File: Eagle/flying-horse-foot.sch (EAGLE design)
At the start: 20 parts, among them U1 8U2-AU, Y1 16MHz

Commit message: rel 1
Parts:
- added S1: MK6-5-B, switch-reed:REED-SWITCH-MK6-5-B
- C4, C6: value 0.1uF -> 1.0uF; device SparkFun-Capacitors:0.1UF-0603-25V-5% -> SparkFun-Capacitors:1.0UF-0603-16V-10%
- C7, C8: value 1.0uF -> 0.1uF; device SparkFun-Capacitors:1.0UF-0603-16V-10% -> SparkFun-Capacitors:0.1UF-0603-25V-5%
- U$1, U$2: value 74HC42 -> 74HC42D16; device aaa2:74HC42 -> aaa2:74HC42D16
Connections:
- removed net N$9: RESET.2, U1.RESET/PC1
- new net RESET: RESET.2, S1.1, U1.RESET/PC1
- net COL-3: no longer U$4.P$13
- net COL-5: now also U$4.P$13
- net GND: now also C5.1, C8.2, S1.2; no longer C5.2, C8.1
- net N$3: now also C2.1; no longer C3.1
- net N$4: now also C3.1; no longer C2.1
- net N$6: now also C4.1; no longer C7.1
- net VCC: now also C5.2, C7.1, C8.1; no longer C4.1, C5.1, C8.2
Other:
- moved on the sheet: C2, C3, C4, C5, C6, C7, C8, R4, R5, RESET

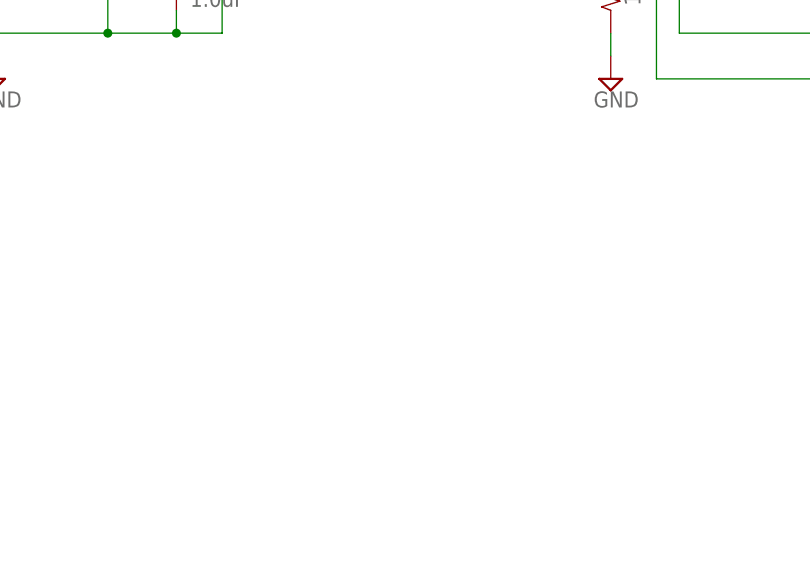
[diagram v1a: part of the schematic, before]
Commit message: made top plane vcc, instead of gnd
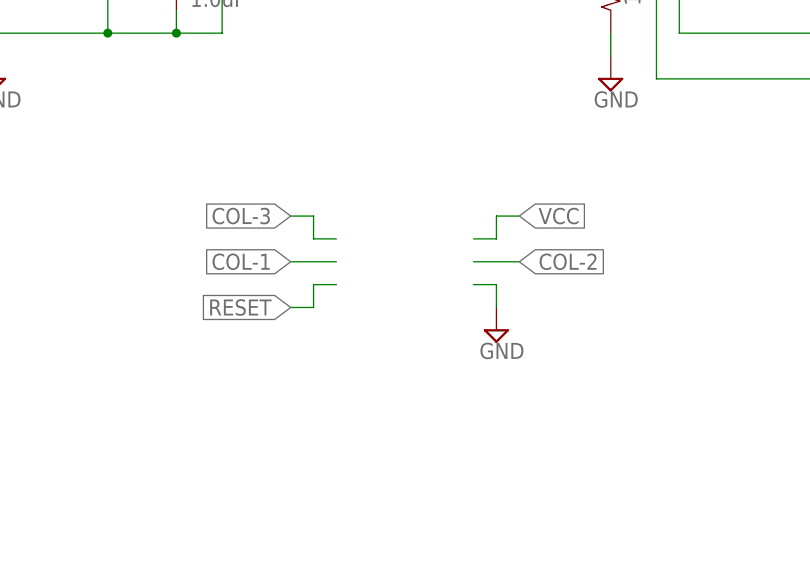
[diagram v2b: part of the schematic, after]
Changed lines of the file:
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@@
 <part name="SUPPLY6" library="supply2" library_urn="urn:adsk.eagle:library:372" deviceset="GND" device=""/>
 <part name="S1" library="switch-reed" library_urn="urn:adsk.eagle:library:379" deviceset="REED-SWITCH-" device="MK6-5-B" package3d_urn="urn:adsk.eagle:package:27524/1" value="MK6-5-B"/>
+<part name="SUPPLY7" library="supply2" library_urn="urn:adsk.eagle:library:372" deviceset="GND" device=""/>
 </parts>
 <sheets>
@@
 <attribute name="NAME" x="160.02" y="167.64" size="1.778" layer="95" rot="R270"/>
 <attribute name="VALUE" x="157.48" y="167.64" size="1.778" layer="96" rot="R270"/>
+</instance>
+<instance part="SUPPLY7" gate="GND" x="208.28" y="43.18" smashed="yes">
+<attribute name="VALUE" x="206.375" y="40.005" size="1.778" layer="96"/>
 </instance>
 </instances>
@@
 <junction x="152.4" y="154.94"/>
 </segment>
+<segment>
+<wire x1="205.74" y1="48.26" x2="208.28" y2="48.26" width="0.1524" layer="91"/>
+<pinref part="SUPPLY7" gate="GND" pin="GND"/>
+<wire x1="208.28" y1="48.26" x2="208.28" y2="45.72" width="0.1524" layer="91"/>
+</segment>
 </net>
 <net name="ROW-B" class="0">
@@
 <pinref part="U$4" gate="G$1" pin="P$5"/>
 </segment>
+<segment>
+<wire x1="205.74" y1="50.8" x2="210.82" y2="50.8" width="0.1524" layer="91"/>
+<label x="210.82" y="50.8" size="1.778" layer="95" xref="yes"/>
+</segment>
 </net>
 <net name="COL-0" class="0">
@@
 <pinref part="U$4" gate="G$1" pin="P$8"/>
 </segment>
+<segment>
+<wire x1="190.5" y1="53.34" x2="187.96" y2="53.34" width="0.1524" layer="91"/>
+<wire x1="187.96" y1="53.34" x2="187.96" y2="55.88" width="0.1524" layer="91"/>
+<wire x1="187.96" y1="55.88" x2="185.42" y2="55.88" width="0.1524" layer="91"/>
+<label x="185.42" y="55.88" size="1.778" layer="95" rot="R180" xref="yes"/>
+</segment>
 </net>
 <net name="COL-1" class="0">
@@
 <label x="45.72" y="78.74" size="1.778" layer="95" xref="yes"/>
 <pinref part="U$4" gate="G$1" pin="P$3"/>
+</segment>
+<segment>
+<wire x1="190.5" y1="50.8" x2="185.42" y2="50.8" width="0.1524" layer="91"/>
+<label x="185.42" y="50.8" size="1.778" layer="95" rot="R180" xref="yes"/>
 </segment>
 </net>
@@
 <junction x="78.74" y="60.96"/>
 </segment>
+<segment>
+<wire x1="205.74" y1="53.34" x2="208.28" y2="53.34" width="0.1524" layer="91"/>
+<wire x1="208.28" y1="53.34" x2="208.28" y2="55.88" width="0.1524" layer="91"/>
+<wire x1="208.28" y1="55.88" x2="210.82" y2="55.88" width="0.1524" layer="91"/>
+<label x="210.82" y="55.88" size="1.778" layer="95" xref="yes"/>
+</segment>
 </net>
 <net name="N$1" class="0">
@@
 <label x="177.8" y="165.1" size="1.778" layer="95" xref="yes"/>
 </segment>
-</net>
+<segment>
+<wire x1="190.5" y1="48.26" x2="187.96" y2="48.26" width="0.1524" layer="91"/>
+<wire x1="187.96" y1="48.26" x2="187.96" y2="45.72" width="0.1524" layer="91"/>
+<wire x1="187.96" y1="45.72" x2="185.42" y2="45.72" width="0.1524" layer="91"/>
+<label x="185.42" y="45.72" size="1.778" layer="95" rot="R180" xref="yes"/>
+</segment>
+</net>

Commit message: prep for board manufacturing
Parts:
- removed Y1: 16MHz, SparkFun-Clocks:CRYSTAL-16MHZSMD-2X1.6
- added Y2: 16MHz, SparkFun-Clocks:CRYSTAL-16MHZSMD-5X3.2
- C1: device SparkFun-Capacitors:10UF-POLAR-EIA3216-16V-10%(TANT) -> aaa2:EEE-1CA100SR-EIA3528-20V-10%(TANT)
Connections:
- net N$3: now also Y2.2; no longer Y1.2
- net N$4: now also Y2.1; no longer Y1.1

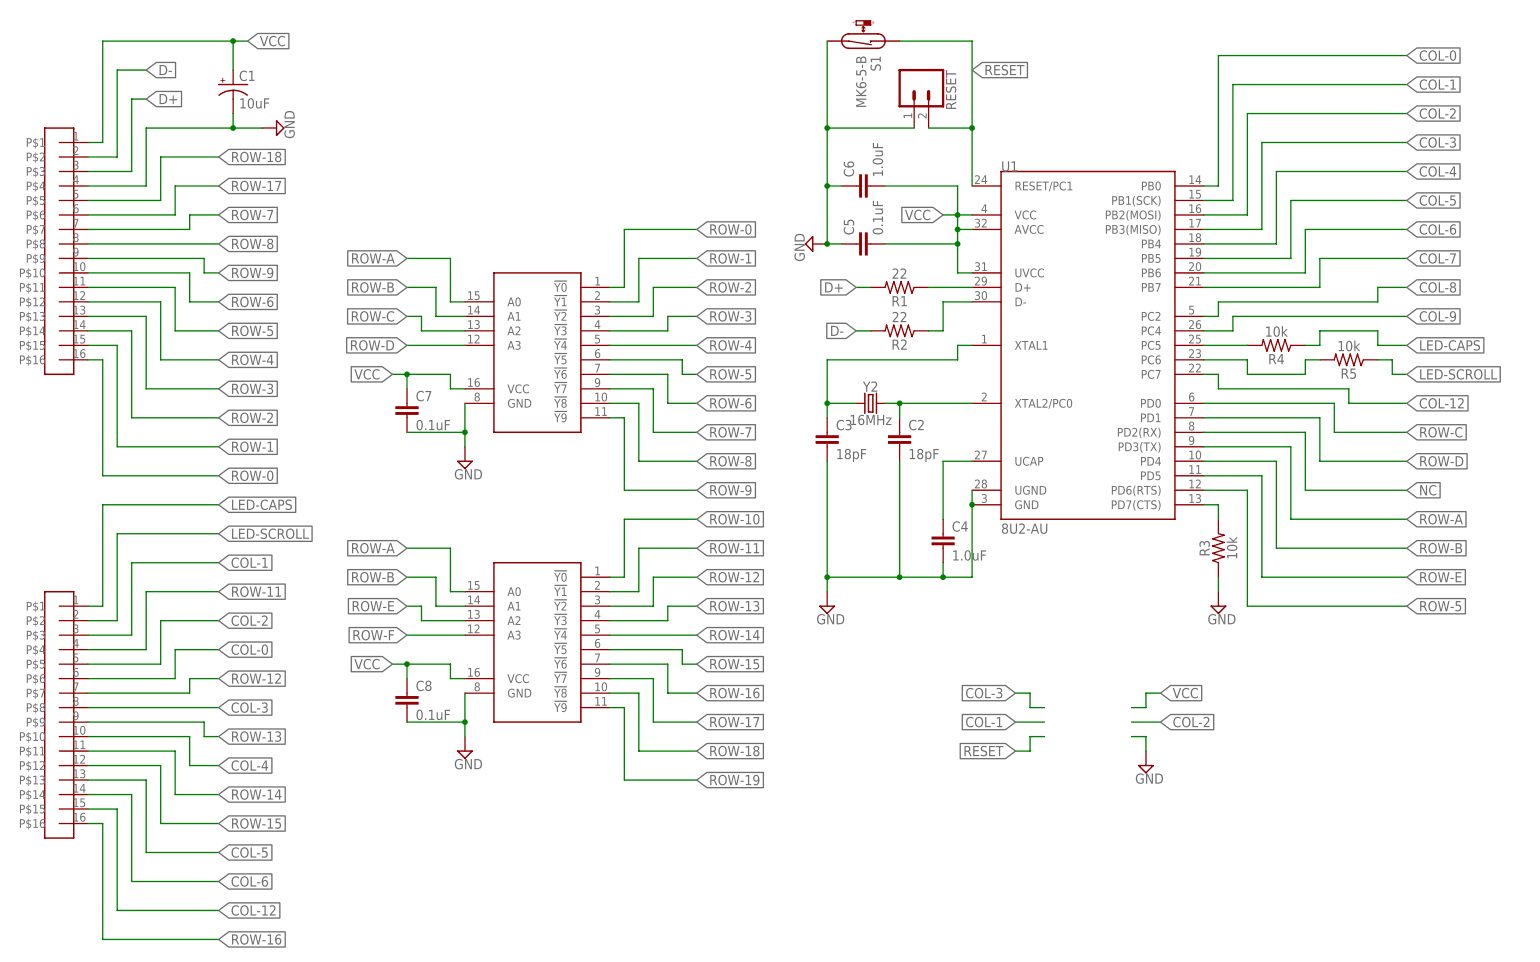
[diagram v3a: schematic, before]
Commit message: Added SPI6 header for easier AVR programming
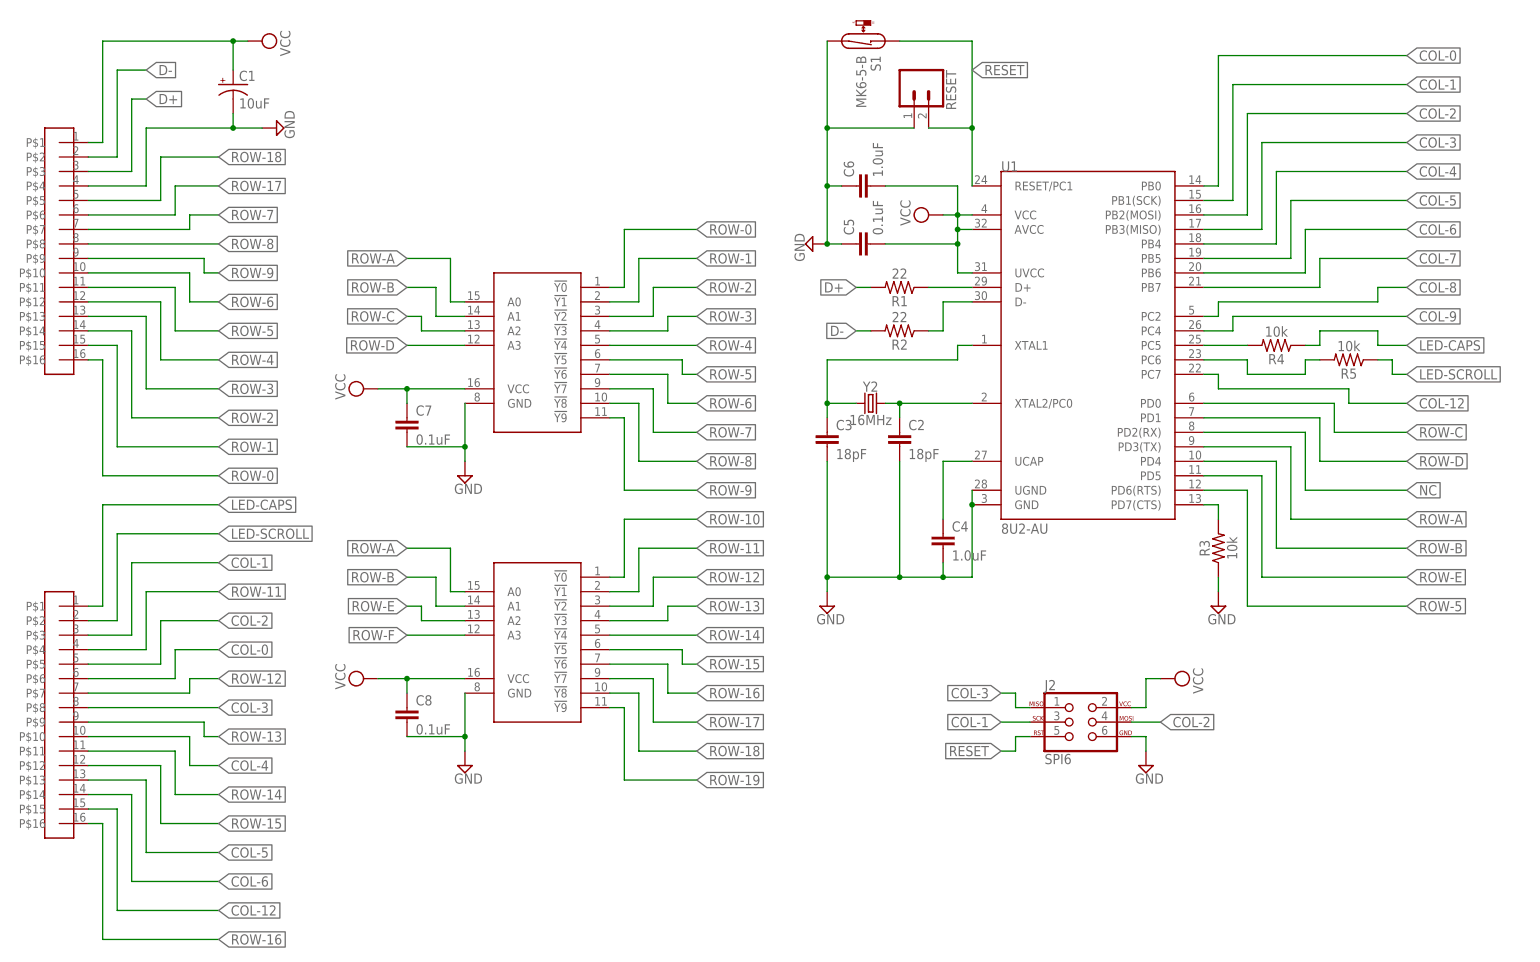
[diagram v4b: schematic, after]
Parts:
- added J2: SPI6, SparkFun-Connectors:AVR_SPI_PROG_3X2NS
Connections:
- net COL-1: now also J2.3
- net COL-2: now also J2.4
- net COL-3: now also J2.1
- net GND: now also J2.6
- net RESET: now also J2.5
- net VCC: now also J2.2
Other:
- moved on the sheet: C7, C8

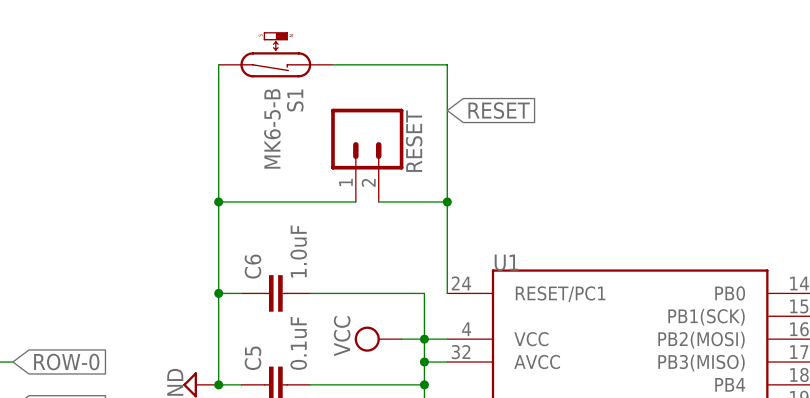
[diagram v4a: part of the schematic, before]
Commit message: Added jumper to disable magnetic reed switch
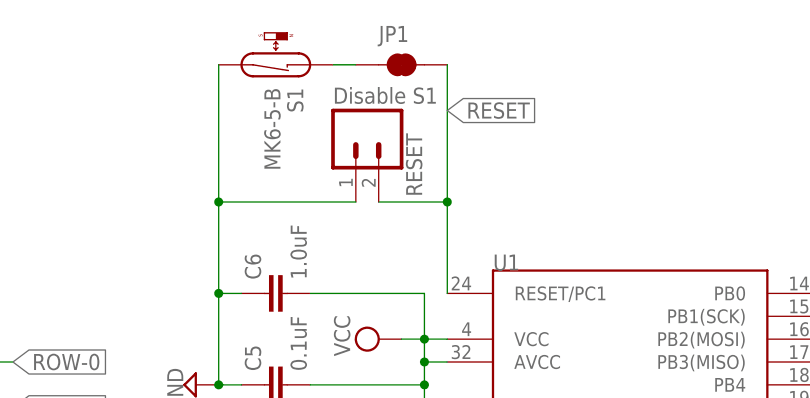
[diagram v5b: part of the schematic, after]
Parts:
- added JP1: Disable S1, SparkFun-Jumpers:JUMPER-SMT_2_NC_TRACE_NO-SILK
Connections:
- new net N$8: JP1.1, S1.1
- net RESET: now also JP1.2; no longer S1.1
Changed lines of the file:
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@@
 <part name="SUPPLY12" library="supply2" library_urn="urn:adsk.eagle:library:372" deviceset="VCC" device=""/>
 <part name="J2" library="SparkFun-Connectors" deviceset="AVR_SPI_PROG_3X2" device="NS" value="SPI6"/>
+<part name="JP1" library="SparkFun-Jumpers" deviceset="JUMPER-SMT_2_NC_TRACE" device="_NO-SILK" package3d_urn="urn:adsk.eagle:package:39286/1" value="Disable S1"/>
 </parts>
 <sheets>
@@
 <instance part="RESET" gate="G$1" x="167.64" y="162.56" smashed="yes" rot="R270">
 <attribute name="VALUE" x="162.814" y="165.1" size="1.778" layer="96" font="vector" rot="R270"/>
-<attribute name="NAME" x="173.228" y="165.1" size="1.778" layer="95" font="vector" rot="R270"/>
+<attribute name="NAME" x="173.228" y="162.56" size="1.778" layer="95" font="vector" rot="R270"/>
 </instance>
 <instance part="SUPPLY6" gate="GND" x="149.86" y="134.62" smashed="yes" rot="R270">
@@
 <attribute name="NAME" x="190.5" y="56.388" size="1.778" layer="95" font="vector"/>
 <attribute name="VALUE" x="190.5" y="43.434" size="1.778" layer="96" font="vector"/>
+</instance>
+<instance part="JP1" gate="G$1" x="172.72" y="170.18" smashed="yes">
+<attribute name="NAME" x="170.18" y="172.72" size="1.778" layer="95" font="vector"/>
+<attribute name="VALUE" x="165.1" y="167.64" size="1.778" layer="96" font="vector" align="top-left"/>
 </instance>
 </instances>
@@
 <pinref part="U1" gate="G$1" pin="RESET/PC1"/>
 <wire x1="177.8" y1="154.94" x2="177.8" y2="144.78" width="0.1524" layer="91"/>
-<pinref part="S1" gate="G$1" pin="1"/>
-<wire x1="165.1" y1="170.18" x2="177.8" y2="170.18" width="0.1524" layer="91"/>
 <wire x1="177.8" y1="170.18" x2="177.8" y2="154.94" width="0.1524" layer="91"/>
 <junction x="177.8" y="154.94"/>
 <label x="177.8" y="165.1" size="1.778" layer="95" xref="yes"/>
+<pinref part="JP1" gate="G$1" pin="2"/>
 </segment>
 <segment>
@@
 </segment>
 </net>
+<net name="N$8" class="0">
+<segment>
+<pinref part="S1" gate="G$1" pin="1"/>
+<pinref part="JP1" gate="G$1" pin="1"/>
+<wire x1="167.64" y1="170.18" x2="165.1" y2="170.18" width="0.1524" layer="91"/>
+</segment>
+</net>
 </nets>
 </sheet>
 </sheets>
+<errors>
+</errors>
 </schematic>
 </drawing>
